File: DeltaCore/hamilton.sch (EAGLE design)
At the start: 68 parts, among them Q1 CSD16301Q2, Q2 CSD16301Q2, Q3 MOSFET-NCHANNEL_SOT23-3, Q4 MOSFET-NCHANNEL_SOT23-3, Q5 MOSFET-NCHANNEL_SOT23-3, Q6 MOSFET-NCHANNEL_SOT23-3, Q7 NFET_AON7408, Q8 NFET_AON7408, U1 SAMR21, U10 PCA9557, U2 APDS9007, U3 MMA7660FC, U4 AT30TS74, U5 MCP73871-2AAI/ML, U7 BQ29718, U8 MCP1824ST-3302E/DB, U9 TPS61090, X1 XTAL

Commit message: more
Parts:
- removed R3: 20k, storm:0603_RESISTORSMALL
- removed U2: APDS9007, storm:APDS9007
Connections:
- net +3V3: no longer U2.VCC, U5.*TE, U5.CE, U5.PROG2, U5.SEL
- net GND: no longer R3.P$1, U2.GND
- net LS: no longer R3.P$2, U2.OUT
- net SD: no longer U2.SD
- net VCC: now also U5.*TE, U5.CE, U5.PROG2, U5.SEL
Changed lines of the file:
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@@
 <part name="SUPPLY3" library="supply2" deviceset="GND" device=""/>
 <part name="SUPPLY4" library="supply2" deviceset="GND" device=""/>
-<part name="U2" library="storm" deviceset="APDS9007" device=""/>
 <part name="U3" library="storm" deviceset="MMA7660FC" device=""/>
 <part name="R1" library="storm" deviceset="0603_RESISTOR" device="SMALL" value="3k6"/>
@@
 <part name="+3V2" library="supply1" deviceset="+3V3" device=""/>
 <part name="+3V3" library="supply1" deviceset="+3V3" device=""/>
-<part name="+3V4" library="supply1" deviceset="+3V3" device=""/>
 <part name="SUPPLY5" library="supply2" deviceset="GND" device=""/>
-<part name="SUPPLY6" library="supply2" deviceset="GND" device=""/>
 <part name="SUPPLY7" library="supply2" deviceset="GND" device=""/>
-<part name="R3" library="storm" deviceset="0603_RESISTOR" device="SMALL" value="20k"/>
 <part name="U$1" library="storm" deviceset="JLINK_CONNECT" device=""/>
 <part name="SUPPLY8" library="supply2" deviceset="GND" device=""/>
@@
 <instance part="SUPPLY3" gate="GND" x="-10.16" y="50.8"/>
 <instance part="SUPPLY4" gate="GND" x="0" y="50.8"/>
-<instance part="U2" gate="G$1" x="114.3" y="68.58"/>
 <instance part="U3" gate="G$1" x="114.3" y="35.56"/>
 <instance part="R1" gate="G$1" x="139.7" y="40.64" smashed="yes" rot="R90">
@@
 <instance part="+3V2" gate="G$1" x="93.98" y="43.18"/>
 <instance part="+3V3" gate="G$1" x="134.62" y="45.72"/>
-<instance part="+3V4" gate="G$1" x="99.06" y="76.2"/>
 <instance part="SUPPLY5" gate="GND" x="93.98" y="30.48"/>
-<instance part="SUPPLY6" gate="GND" x="129.54" y="55.88"/>
 <instance part="SUPPLY7" gate="GND" x="137.16" y="27.94"/>
-<instance part="R3" gate="G$1" x="134.62" y="66.04" smashed="yes" rot="R90">
-<attribute name="NAME" x="138.43" y="66.548" size="1.27" layer="95" rot="R180"/>
-<attribute name="VALUE" x="138.938" y="65.024" size="1.27" layer="96" rot="R180"/>
-</instance>
 <instance part="U$1" gate="G$1" x="81.28" y="86.36"/>
 <instance part="SUPPLY8" gate="GND" x="53.34" y="81.28" rot="R270"/>
@@
 </segment>
 <segment>
-<pinref part="U2" gate="G$1" pin="GND"/>
-<wire x1="127" y1="66.04" x2="129.54" y2="63.5" width="0.1524" layer="91"/>
-<pinref part="SUPPLY6" gate="GND" pin="GND"/>
-<wire x1="129.54" y1="63.5" x2="129.54" y2="60.96" width="0.1524" layer="91"/>
-<pinref part="R3" gate="G$1" pin="P$1"/>
-<wire x1="129.54" y1="60.96" x2="129.54" y2="58.42" width="0.1524" layer="91"/>
-<wire x1="134.62" y1="60.96" x2="129.54" y2="60.96" width="0.1524" layer="91"/>
-<junction x="129.54" y="60.96"/>
-</segment>
-<segment>
 <pinref part="U$1" gate="G$1" pin="GND"/>
 <pinref part="SUPPLY8" gate="GND" pin="GND"/>
@@
 </segment>
 <segment>
-<pinref part="U2" gate="G$1" pin="VCC"/>
-<wire x1="101.6" y1="68.58" x2="99.06" y2="71.12" width="0.1524" layer="91"/>
-<pinref part="+3V4" gate="G$1" pin="+3V3"/>
-<wire x1="99.06" y1="71.12" x2="99.06" y2="73.66" width="0.1524" layer="91"/>
-</segment>
-<segment>
 <pinref part="U3" gate="G$1" pin="DVDD"/>
 <pinref part="+3V3" gate="G$1" pin="+3V3"/>
@@
 <label x="-187.96" y="-160.02" size="1.778" layer="95" rot="R180" xref="yes"/>
 </segment>
-<segment>
-<pinref part="U5" gate="A" pin="SEL"/>
-<wire x1="-116.84" y1="-40.64" x2="-121.92" y2="-40.64" width="0.1524" layer="91"/>
-<wire x1="-121.92" y1="-40.64" x2="-121.92" y2="-43.18" width="0.1524" layer="91"/>
-<pinref part="U5" gate="A" pin="PROG2"/>
-<wire x1="-121.92" y1="-43.18" x2="-116.84" y2="-43.18" width="0.1524" layer="91"/>
-<pinref part="U5" gate="A" pin="*TE"/>
-<wire x1="-116.84" y1="-45.72" x2="-121.92" y2="-45.72" width="0.1524" layer="91"/>
-<wire x1="-121.92" y1="-45.72" x2="-121.92" y2="-43.18" width="0.1524" layer="91"/>
-<junction x="-121.92" y="-43.18"/>
-<pinref part="U5" gate="A" pin="CE"/>
-<wire x1="-116.84" y1="-48.26" x2="-121.92" y2="-48.26" width="0.1524" layer="91"/>
-<wire x1="-121.92" y1="-48.26" x2="-121.92" y2="-45.72" width="0.1524" layer="91"/>
-<junction x="-121.92" y="-45.72"/>
-<wire x1="-121.92" y1="-48.26" x2="-127" y2="-48.26" width="0.1524" layer="91"/>
-<junction x="-121.92" y="-48.26"/>
-<label x="-127" y="-48.26" size="1.778" layer="95" rot="R180" xref="yes"/>
-</segment>
 </net>
 <net name="SWDIO" class="0">
@@
 <label x="30.48" y="35.56" size="1.27" layer="95" rot="R180" xref="yes"/>
 </segment>
-<segment>
-<pinref part="U2" gate="G$1" pin="OUT"/>
-<wire x1="127" y1="68.58" x2="134.62" y2="68.58" width="0.1524" layer="91"/>
-<pinref part="R3" gate="G$1" pin="P$2"/>
-<wire x1="134.62" y1="68.58" x2="147.32" y2="68.58" width="0.1524" layer="91"/>
-<junction x="134.62" y="68.58"/>
-<label x="147.32" y="68.58" size="1.27" layer="95" xref="yes"/>
-</segment>
 </net>
 <net name="ACC" class="0">
@@
 </net>
 <net name="SD" class="0">
-<segment>
-<pinref part="U2" gate="G$1" pin="SD"/>
-<wire x1="101.6" y1="66.04" x2="99.06" y2="66.04" width="0.1524" layer="91"/>
-<label x="99.06" y="66.04" size="1.27" layer="95" rot="R180" xref="yes"/>
-</segment>
 <segment>
 <pinref part="U1" gate="G$1" pin="PA28"/>
@@
 <pinref part="U5" gate="A" pin="IN"/>
 </segment>
-</net>
+<segment>
+<pinref part="U5" gate="A" pin="SEL"/>
+<wire x1="-116.84" y1="-40.64" x2="-121.92" y2="-40.64" width="0.1524" layer="91"/>
+<wire x1="-121.92" y1="-40.64" x2="-121.92" y2="-43.18" width="0.1524" layer="91"/>
+<pinref part="U5" gate="A" pin="PROG2"/>
+<wire x1="-121.92" y1="-43.18" x2="-116.84" y2="-43.18" width="0.1524" layer="91"/>
+<pinref part="U5" gate="A" pin="*TE"/>
+<wire x1="-116.84" y1="-45.72" x2="-121.92" y2="-45.72" width="0.1524" layer="91"/>
+<wire x1="-121.92" y1="-45.72" x2="-121.92" y2="-43.18" width="0.1524" layer="91"/>
+<junction x="-121.92" y="-43.18"/>
+<pinref part="U5" gate="A" pin="CE"/>
+<wire x1="-116.84" y1="-48.26" x2="-121.92" y2="-48.26" width="0.1524" layer="91"/>
+<wire x1="-121.92" y1="-48.26" x2="-121.92" y2="-45.72" width="0.1524" layer="91"/>
+<junction x="-121.92" y="-45.72"/>
+<wire x1="-121.92" y1="-48.26" x2="-127" y2="-48.26" width="0.1524" layer="91"/>
+<junction x="-121.92" y="-48.26"/>
+<label x="-127" y="-48.26" size="1.778" layer="95" rot="R180" xref="yes"/>
+</segment>
+</net>

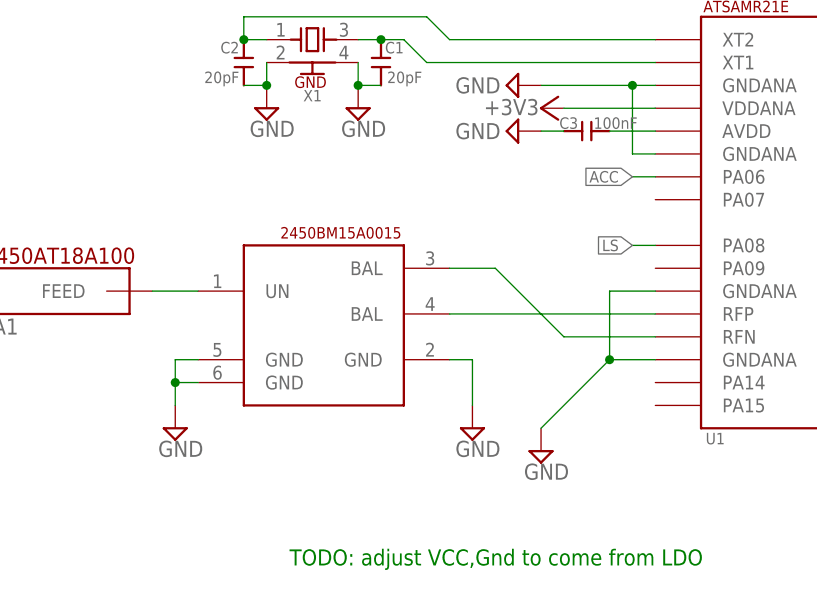
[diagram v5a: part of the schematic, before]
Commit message: add analog line for fan
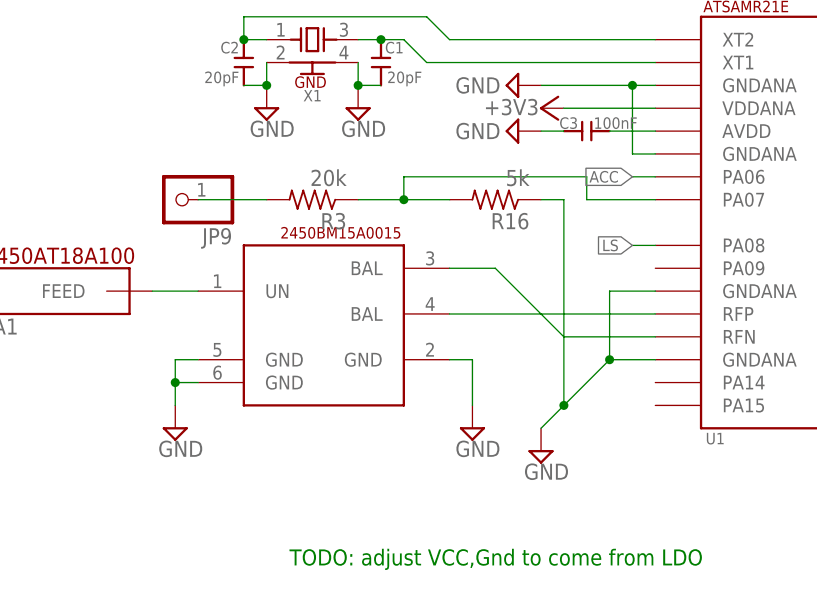
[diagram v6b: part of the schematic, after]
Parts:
- added JP9: (no value), pinhead:PINHD-1X1
- added R16: 5k, resistor:R-US_R0402
- added R3: 20k, resistor:R-US_R0402
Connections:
- new net N$8: JP9.1, R3.2
- new net N$9: R16.2, R3.1, U1.PA07
- net GND: now also R16.1
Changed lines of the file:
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@@
 <part name="R4" library="resistor" deviceset="R-US_" device="R0603" value="??"/>
 <part name="R15" library="resistor" deviceset="R-US_" device="R0603" value="??"/>
+<part name="JP9" library="pinhead" deviceset="PINHD-1X1" device=""/>
+<part name="R3" library="resistor" deviceset="R-US_" device="R0402" value="20k"/>
+<part name="R16" library="resistor" deviceset="R-US_" device="R0402" value="5k"/>
 </parts>
 <sheets>
@@
 <instance part="R4" gate="G$1" x="-157.48" y="-30.48" rot="R90"/>
 <instance part="R15" gate="G$1" x="-157.48" y="-45.72" rot="R90"/>
+<instance part="JP9" gate="G$1" x="-20.32" y="40.64" rot="R180"/>
+<instance part="R3" gate="G$1" x="-5.08" y="40.64" rot="R180"/>
+<instance part="R16" gate="G$1" x="15.24" y="40.64" rot="R180"/>
 </instances>
 <busses>
@@
 <wire x1="27.94" y1="30.48" x2="27.94" y2="22.86" width="0.1524" layer="91"/>
 <pinref part="U1" gate="G$1" pin="GNDANA@14"/>
-<wire x1="27.94" y1="22.86" x2="20.32" y2="15.24" width="0.1524" layer="91"/>
+<wire x1="27.94" y1="22.86" x2="22.86" y2="17.78" width="0.1524" layer="91"/>
+<wire x1="22.86" y1="17.78" x2="20.32" y2="15.24" width="0.1524" layer="91"/>
 <wire x1="33.02" y1="22.86" x2="27.94" y2="22.86" width="0.1524" layer="91"/>
 <junction x="27.94" y="22.86"/>
 <pinref part="SUPPLY10" gate="GND" pin="GND"/>
+<pinref part="R16" gate="G$1" pin="1"/>
+<wire x1="20.32" y1="40.64" x2="22.86" y2="40.64" width="0.1524" layer="91"/>
+<wire x1="22.86" y1="40.64" x2="22.86" y2="17.78" width="0.1524" layer="91"/>
+<junction x="22.86" y="17.78"/>
 </segment>
 <segment>
@@
 </segment>
 </net>
+<net name="N$8" class="0">
+<segment>
+<pinref part="JP9" gate="G$1" pin="1"/>
+<pinref part="R3" gate="G$1" pin="2"/>
+<wire x1="-17.78" y1="40.64" x2="-10.16" y2="40.64" width="0.1524" layer="91"/>
+</segment>
+</net>
+<net name="N$9" class="0">
+<segment>
+<pinref part="R3" gate="G$1" pin="1"/>
+<pinref part="R16" gate="G$1" pin="2"/>
+<wire x1="0" y1="40.64" x2="5.08" y2="40.64" width="0.1524" layer="91"/>
+<wire x1="5.08" y1="40.64" x2="10.16" y2="40.64" width="0.1524" layer="91"/>
+<wire x1="5.08" y1="40.64" x2="5.08" y2="43.18" width="0.1524" layer="91"/>
+<junction x="5.08" y="40.64"/>
+<wire x1="5.08" y1="43.18" x2="25.4" y2="43.18" width="0.1524" layer="91"/>
+<wire x1="25.4" y1="43.18" x2="25.4" y2="40.64" width="0.1524" layer="91"/>
+<pinref part="U1" gate="G$1" pin="PA07"/>
+<wire x1="25.4" y1="40.64" x2="33.02" y2="40.64" width="0.1524" layer="91"/>
+</segment>
+</net>

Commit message: remove TODOs
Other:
- note removed: "NOTE: do not ground until after this point"
- note removed: "TODO: adjust VCC,Gnd to come from LDO"
- note removed: "TODO: adjust vpcc"
- note removed: "TODO: need control lines for the buttons from hamilton"
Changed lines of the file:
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@@
 <text x="-167.64" y="2.54" size="1.778" layer="91">Input from Witricity PRU</text>
 <text x="-142.24" y="-55.88" size="1.778" layer="91">TODO: pull these high</text>
-<text x="-129.54" y="-15.24" size="1.778" layer="91">TODO: adjust vpcc</text>
-<text x="-7.62" y="0" size="1.778" layer="91">TODO: adjust VCC,Gnd to come from LDO</text>
-<text x="-12.7" y="-66.04" size="1.778" layer="91" rot="R180">NOTE: do not ground until after this point</text>
 <text x="-68.58" y="-106.68" size="1.778" layer="91">To hamilton</text>
 <text x="-121.92" y="-83.82" size="1.778" layer="91">LDO power</text>
-<text x="-111.76" y="-76.2" size="1.778" layer="91">TODO: need control lines for the buttons from hamilton</text>
 <text x="60.96" y="-73.66" size="1.778" layer="91">Boost +5V</text>
 <text x="-101.6" y="-7.62" size="1.778" layer="91">Charging</text>

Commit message: todos
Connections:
- removed net LS: U1.PA08
- net OOB: no longer U1.PA27
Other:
- note removed: "TODO: pull these high"
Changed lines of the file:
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@@
 <text x="123.19" y="43.434" size="1.27" layer="95">0x4C</text>
 <text x="-167.64" y="2.54" size="1.778" layer="91">Input from Witricity PRU</text>
-<text x="-142.24" y="-55.88" size="1.778" layer="91">TODO: pull these high</text>
 <text x="-68.58" y="-106.68" size="1.778" layer="91">To hamilton</text>
 <text x="-121.92" y="-83.82" size="1.778" layer="91">LDO power</text>
@@
 </segment>
 </net>
-<net name="LS" class="0">
-<segment>
-<pinref part="U1" gate="G$1" pin="PA08"/>
-<wire x1="33.02" y1="35.56" x2="30.48" y2="35.56" width="0.1524" layer="91"/>
-<label x="30.48" y="35.56" size="1.27" layer="95" rot="R180" xref="yes"/>
-</segment>
-</net>
 <net name="ACC" class="0">
 <segment>
@@
 <net name="OOB" class="0">
 <segment>
-<pinref part="U1" gate="G$1" pin="PA27"/>
-<wire x1="73.66" y1="40.64" x2="76.2" y2="40.64" width="0.1524" layer="91"/>
-<label x="76.2" y="40.64" size="1.27" layer="95" xref="yes"/>
-</segment>
-<segment>
 <pinref part="U$1" gate="G$1" pin="TDO/SWO"/>
